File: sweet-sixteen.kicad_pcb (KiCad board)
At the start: 2 copper layers, 99.5 x 104.5 mm, 82 parts, among them P1 SDA_I, P10 VIN_O, P11 GND_O, P12 SDA_O, P13 CLK_O, P14 LE_O, P15 ~OE_O, P2 CLK_I, P3 LE_I, P4 ~OE_I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

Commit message: digital bus
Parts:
- moved U31 4.33 mm to (48.3, 61.3)
- moved W5 2.66 mm to (64.8, 57.1)
- moved R5 2.38 mm to (47.6, 72.0)
- moved W3 1.61 mm to (64.8, 61.6)
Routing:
- net /~OE: track 0.00 -> 210.2 mm, vias 0 -> 4
- net /LE: track 0.00 -> 191.2 mm, vias 0 -> 10
- net /CLK: track 0.00 -> 173.1 mm, vias 0 -> 10
- net /SDA_45: track 0.00 -> 52.9 mm, vias 0 -> 2
- net /SDA_34: track 0.00 -> 41.6 mm
- net /SD23: track 0.00 -> 41.6 mm
- net /SDA_12: track 0.00 -> 41.6 mm
- net Net-(P14-Pad1): track 0.00 -> 21.5 mm
- net Net-(P12-Pad1): track 0.00 -> 17.5 mm, vias 0 -> 2
- net /SDA_I: track 0.00 -> 16.9 mm
- net Net-(P13-Pad1): track 0.00 -> 15.4 mm, vias 0 -> 2
- net Net-(P15-Pad1): track 0.00 -> 13.2 mm
- net VIN: track 140.6 -> 131.8 mm, vias 9 -> 6
- net /SDA_O: track 0.00 -> 3.38 mm

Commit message: VLED 50 mils
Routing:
- net /VLED: track 0.00 -> 148.5 mm, vias 0 -> 1
- net Net-(JP2-Pad1): track 0.00 -> 7.78 mm
- net VIN: track 131.8 -> 136.6 mm, vias 6 -> 7
- net /SDA_O: track 3.38 -> 2.69 mm

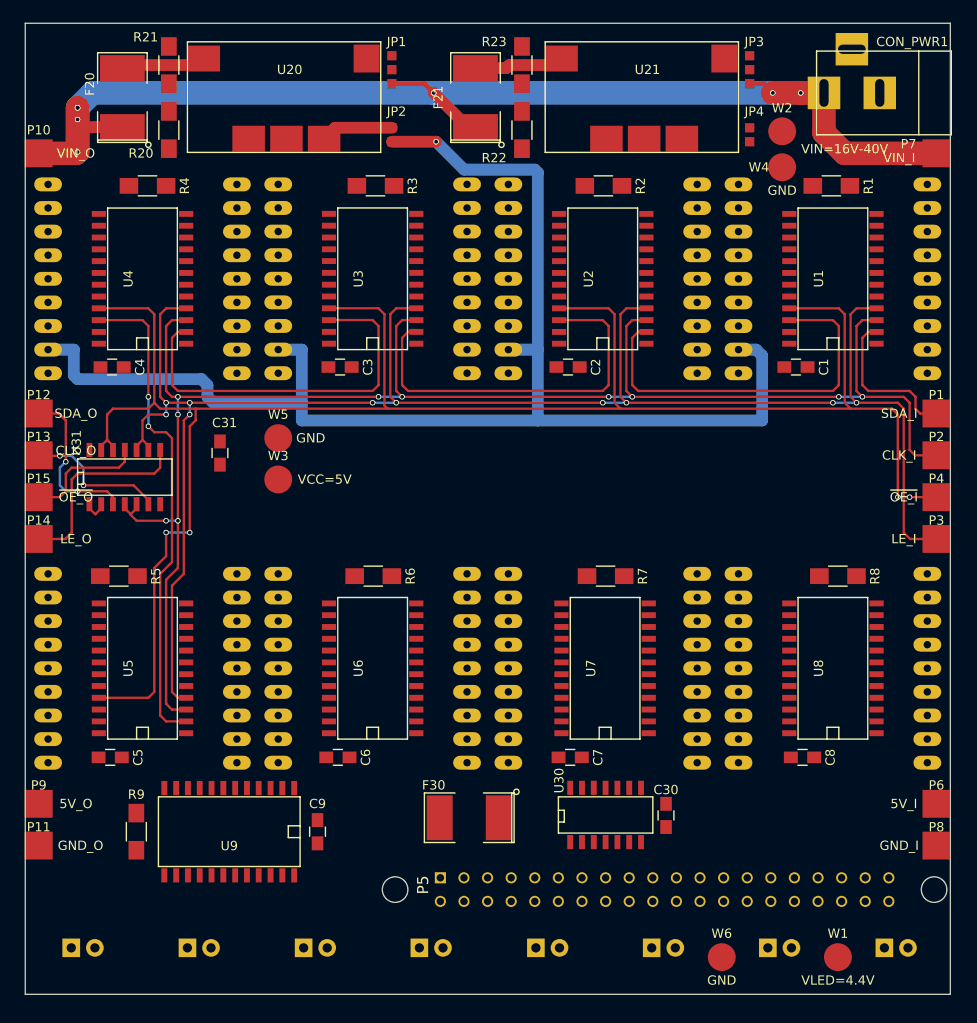
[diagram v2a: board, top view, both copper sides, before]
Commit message: More Power traces
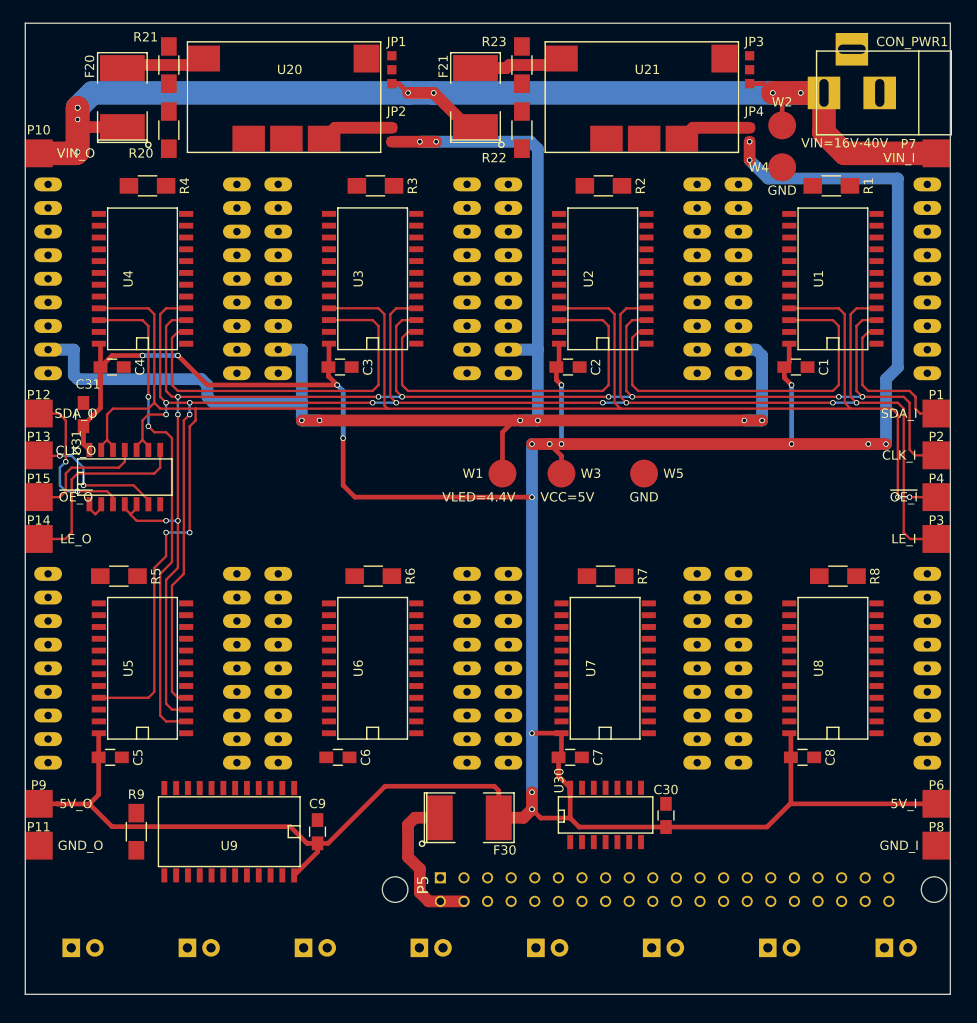
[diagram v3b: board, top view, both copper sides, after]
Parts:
- removed W6: GND, Measurement_Points:Measurement_Point_Round-SMD-Pad_Big
- moved W1 63.3 mm to (88.9, 61.0)
- moved W5 39.6 mm to (104.1, 61.0)
- moved W3 30.5 mm to (95.2, 61.0)
- moved C31 15.3 mm to (43.8, 54.6)
- moved W2 0.63 mm to (119.0, 23.5)
- turned F30 to 0 degrees
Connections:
- U30 pad 8: (no net) -> /SDA_I
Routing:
- net VCC: track 0.00 -> 370.0 mm, vias 0 -> 18
- net /V_PI: track 0.00 -> 16.7 mm
- net /VLED: track 148.5 -> 163.7 mm, vias 1 -> 8
- net Net-(JP4-Pad1): track 0.00 -> 7.78 mm
- net VIN: track 136.6 -> 140.5 mm, vias 7 -> 8

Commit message: rework some parts of the power network on the way fo implement the digital bus
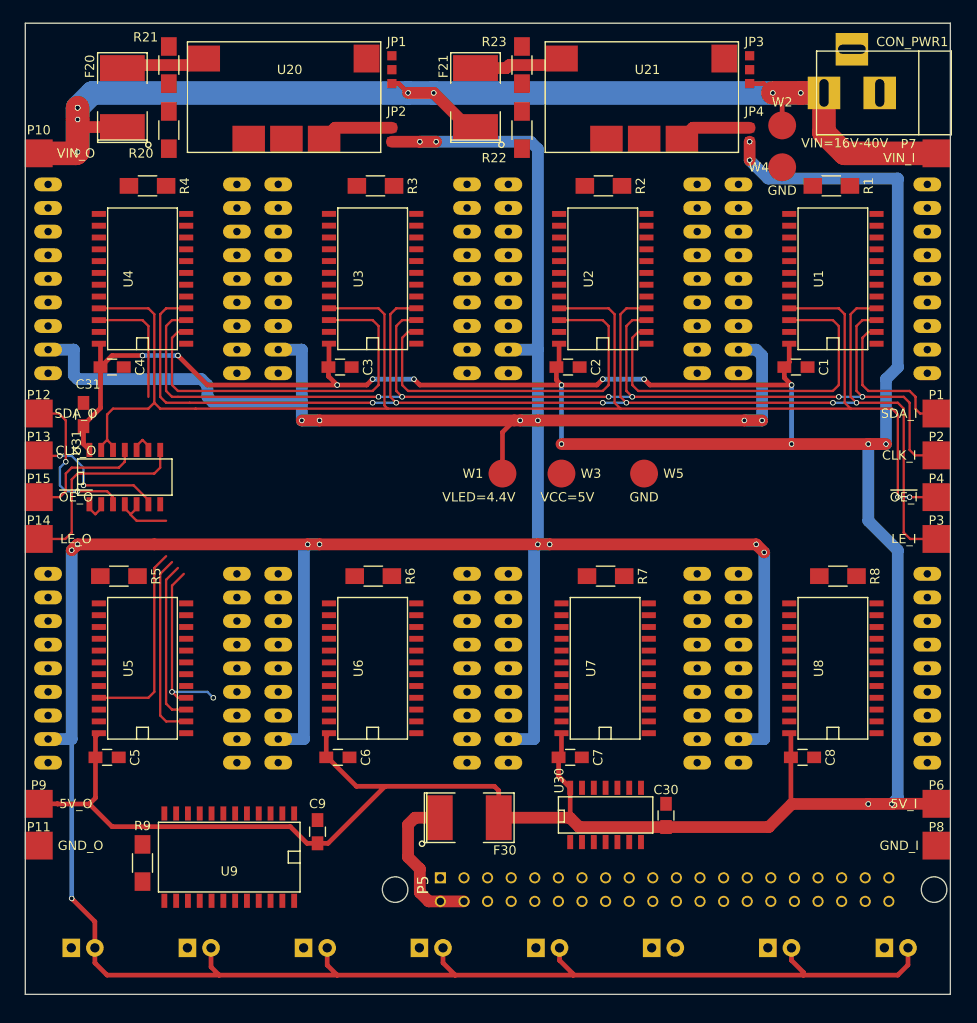
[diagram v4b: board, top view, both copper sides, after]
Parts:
- moved R9 3.43 mm to (50.2, 102.9)
- moved U9 2.73 mm to (59.5, 102.2)
- moved C5 0.34 mm to (46.4, 91.5)
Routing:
- net /VLED: track 163.7 -> 480.8 mm, vias 8 -> 17
- net /LE: track 191.2 -> 171.0 mm, vias 10 -> 8
- net /CLK: track 173.1 -> 153.4 mm, vias 10 -> 6
- net /SDA_45: track 52.9 -> 33.3 mm, vias 2 -> 0
- net /~OE: track 210.2 -> 191.6 mm, vias 4 -> 2
- net VCC: track 370.0 -> 386.7 mm, vias 18 -> 17

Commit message: finished digital and analog net, vled and vcc
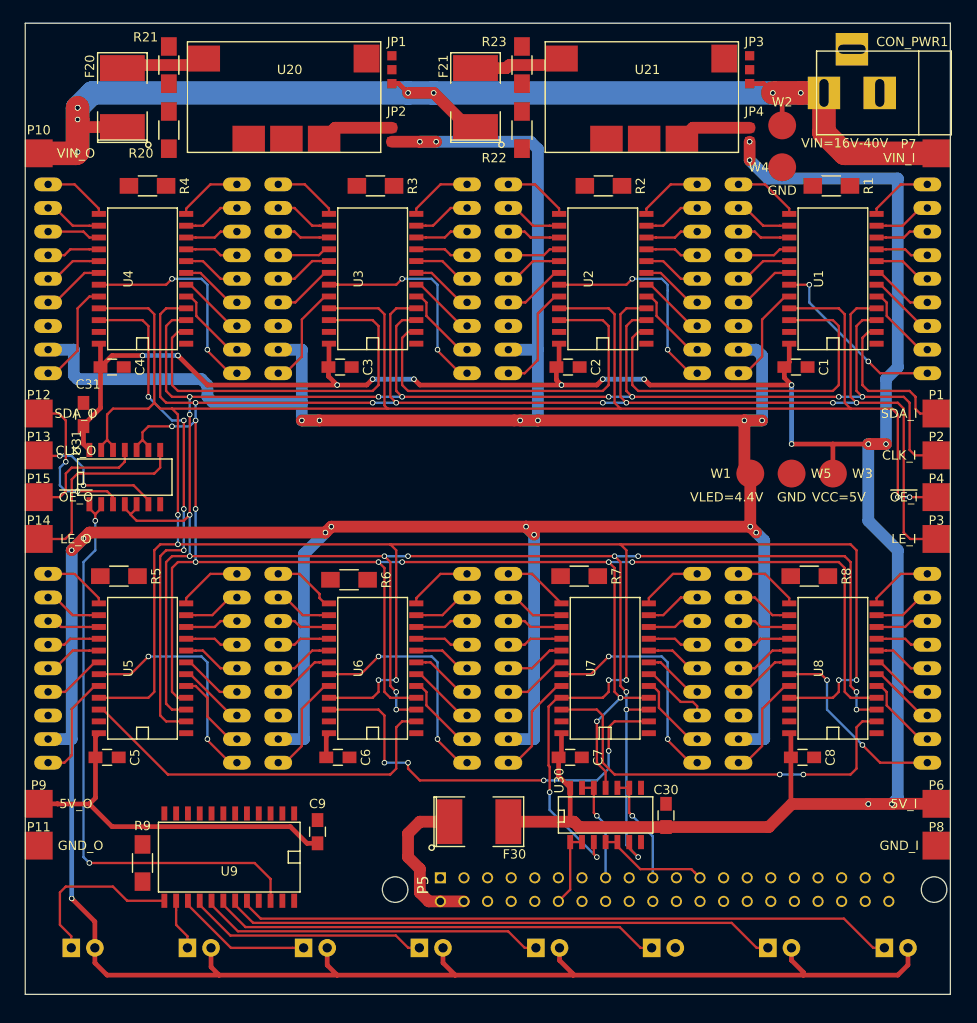
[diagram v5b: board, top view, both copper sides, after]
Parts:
- moved W3 29.2 mm to (124.5, 61.0)
- moved W1 26.7 mm to (115.6, 61.0)
- moved W5 15.9 mm to (120.0, 61.0)
- moved R8 3.08 mm to (121.9, 72.0)
- moved R7 2.84 mm to (97.2, 72.0)
- moved R6 2.64 mm to (72.4, 72.4)
- moved F30 1.12 mm to (86.4, 98.4)
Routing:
- net /~OE: track 191.6 -> 374.3 mm, vias 2 -> 12
- net /CLK: track 153.4 -> 323.0 mm, vias 6 -> 21
- net /LE: track 171.0 -> 327.8 mm, vias 8 -> 17
- net Net-(D8-Pad1): track 0.00 -> 71.0 mm
- net VCC: track 386.7 -> 325.4 mm, vias 17 -> 16
- net /SDA_O: track 2.69 -> 63.6 mm, vias 0 -> 2
- net Net-(D7-Pad1): track 0.00 -> 59.7 mm
- net Net-(D6-Pad1): track 0.00 -> 48.5 mm
- net /SDA_67: track 0.00 -> 46.2 mm, vias 0 -> 4
- net /SDA_78: track 0.00 -> 44.7 mm, vias 0 -> 2
- net /SDA_56: track 0.00 -> 42.0 mm
- net Net-(D5-Pad1): track 0.00 -> 37.3 mm
- net Net-(D4-Pad1): track 0.00 -> 26.0 mm
- net Net-(AFF6-Pad9): track 0.00 -> 25.3 mm, vias 0 -> 2
- net Net-(AFF5-Pad9): track 0.00 -> 25.3 mm, vias 0 -> 2
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
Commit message: route put DP net
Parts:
- moved C5 1.27 mm to (47.6, 91.5)
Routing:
- net Net-(AFF1-Pad12): track 0.00 -> 102.9 mm, vias 0 -> 2
- net Net-(AFF2-Pad12): track 0.00 -> 77.1 mm, vias 0 -> 2
- net Net-(AFF4-Pad12): track 0.00 -> 68.1 mm, vias 0 -> 4
- net /SDA_I: track 16.9 -> 81.5 mm, vias 0 -> 2
- net Net-(AFF3-Pad12): track 0.00 -> 62.3 mm, vias 0 -> 2
- net /SDA_89: track 0.00 -> 59.5 mm, vias 0 -> 1
- net Net-(AFF8-Pad12): track 0.00 -> 52.7 mm
- net VCC: track 325.4 -> 371.6 mm, vias 16 -> 18
- net Net-(AFF7-Pad12): track 0.00 -> 27.7 mm
- net Net-(R9-Pad2): track 0.00 -> 17.9 mm, vias 0 -> 2
- net Net-(AFF5-Pad12): track 0.00 -> 16.8 mm, vias 0 -> 3
- net /CLK: track 323.0 -> 334.9 mm, vias 21 -> 25
- net Net-(AFF6-Pad12): track 0.00 -> 10.9 mm, vias 0 -> 1
- net /~OE: track 374.3 -> 380.3 mm, vias 12 -> 14
- net /VLED: track 479.9 -> 485.2 mm
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- added copper zone on F.Cu, net GND

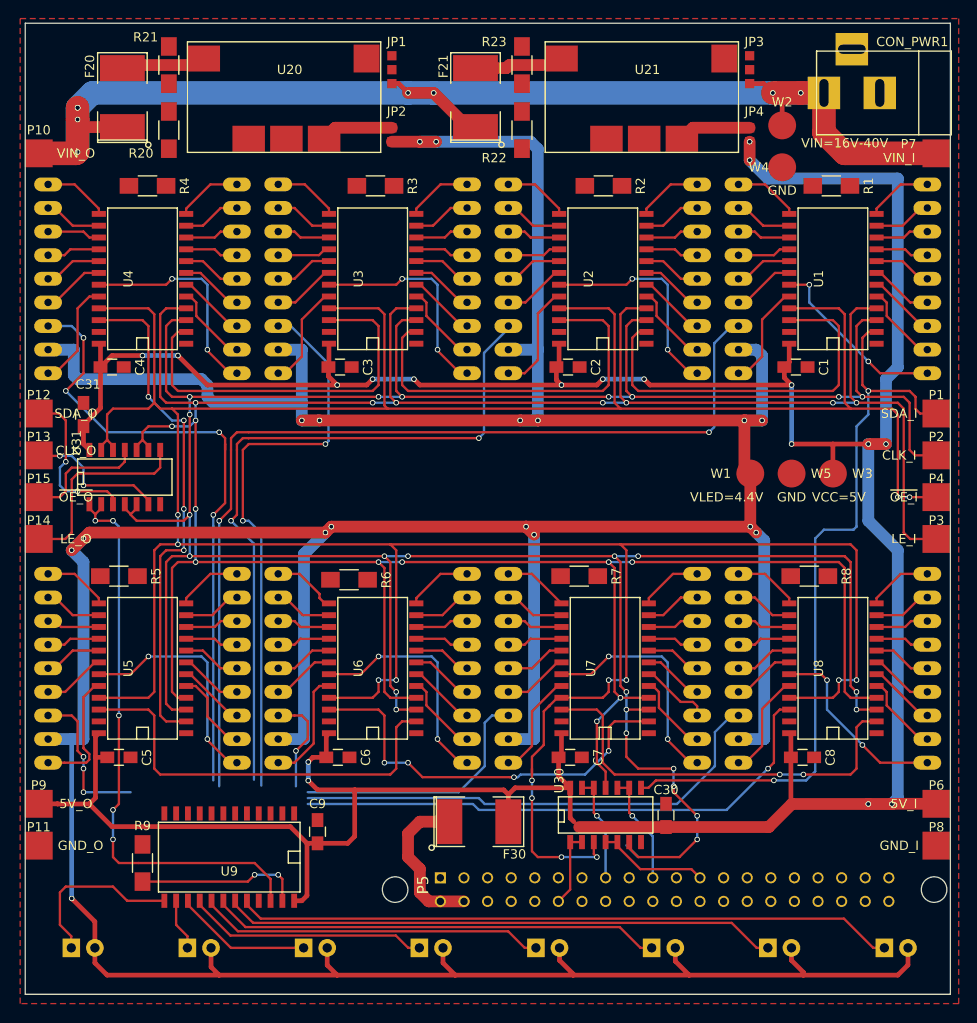
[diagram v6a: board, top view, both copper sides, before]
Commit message: all done but GND
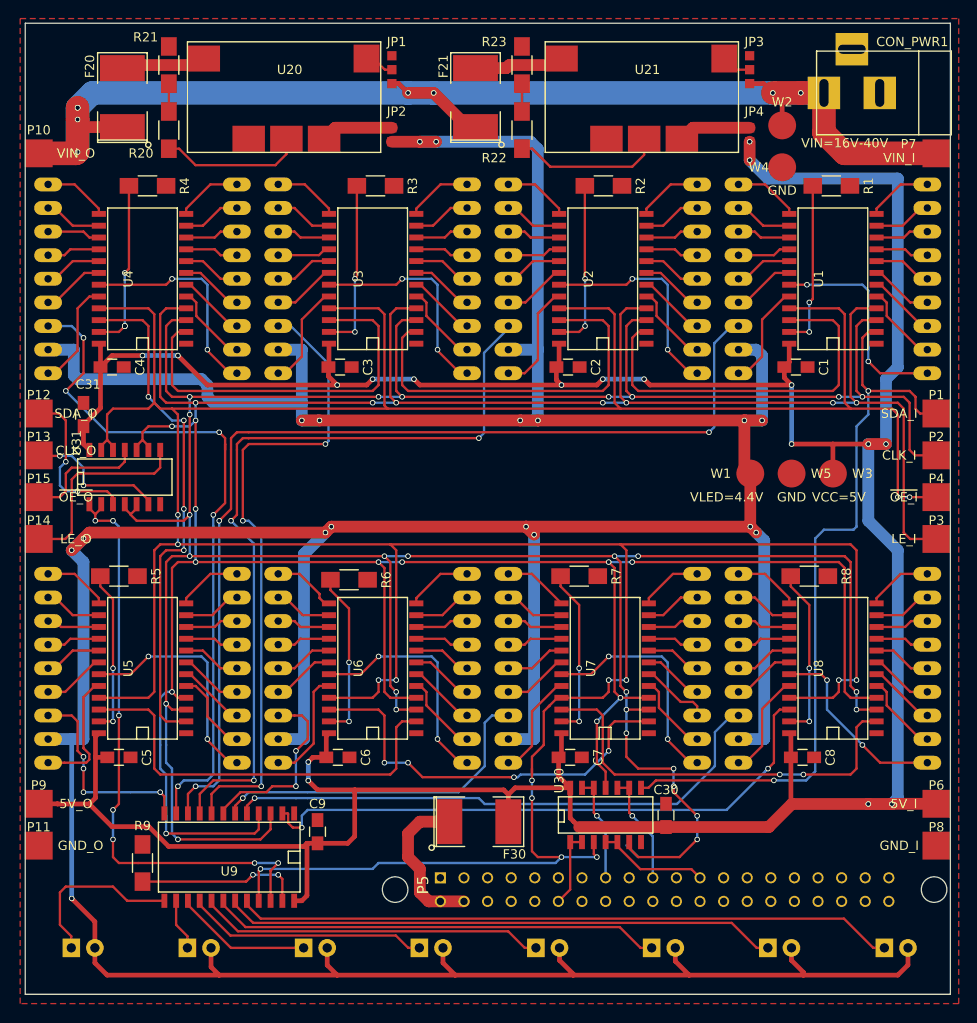
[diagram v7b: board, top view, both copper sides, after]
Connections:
- U9 pad 10: Net-(AFF3-Pad12) -> Net-(AFF1-Pad12)
- U9 pad 11: Net-(AFF2-Pad12) -> Net-(AFF4-Pad12)
- U9 pad 12: Net-(AFF1-Pad12) -> Net-(AFF5-Pad12)
- U9 pad 8: Net-(AFF5-Pad12) -> Net-(AFF3-Pad12)
- U9 pad 9: Net-(AFF4-Pad12) -> Net-(AFF2-Pad12)
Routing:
- net /~OE: track 380.3 -> 416.7 mm, vias 14 -> 15
- net /LE: track 327.8 -> 356.7 mm, vias 17 -> 19
- net /CLK: track 334.9 -> 360.4 mm, vias 25 -> 27
- net Net-(R8-Pad2): track 0.00 -> 18.6 mm, vias 0 -> 2
- net Net-(R3-Pad2): track 0.00 -> 18.6 mm, vias 0 -> 2
- net Net-(R7-Pad2): track 0.00 -> 18.4 mm, vias 0 -> 2
- net Net-(R4-Pad2): track 0.00 -> 18.3 mm, vias 0 -> 4
- net Net-(R6-Pad2): track 0.00 -> 18.2 mm, vias 0 -> 2
- net Net-(R2-Pad2): track 0.00 -> 18.2 mm, vias 0 -> 2
- net Net-(R1-Pad2): track 0.00 -> 18.0 mm, vias 0 -> 2
- net Net-(R5-Pad2): track 0.00 -> 17.7 mm, vias 0 -> 2
- net Net-(R22-Pad2): track 0.00 -> 16.2 mm
- net Net-(R20-Pad2): track 0.00 -> 15.5 mm
- net Net-(AFF6-Pad12): track 10.9 -> 20.2 mm, vias 1 -> 2
- net Net-(AFF7-Pad12): track 27.7 -> 37.0 mm, vias 0 -> 1
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
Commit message: finished gnd routing
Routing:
- net GND: track 0.00 -> 247.0 mm, vias 0 -> 29
- net /CLK: track 360.4 -> 363.9 mm, vias 27 -> 29
- net VCC: track 372.7 -> 370.1 mm, vias 18 -> 16
- net (no net): track 1.80 -> 0.00 mm
- net /SDA_56: track 45.4 -> 45.3 mm, vias 0 -> 4
- added copper zone on B.Cu, net GND
